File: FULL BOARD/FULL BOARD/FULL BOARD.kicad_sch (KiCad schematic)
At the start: 72 parts, among them J1 PJ-036AH-SMT-TR, J2 Micro_SD_Card, J3 Conn_01x04_Male, SW1 SW_Push, U1 LD1117S33TR_SOT223, U2 STM32H743VITx, Y1 16Mhz

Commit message: schematic done
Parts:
- removed FB1: FerriteBead, symbol Device:FerriteBead
- removed J3: Conn_01x04_Male, symbol Connector:Conn_01x04_Male
- removed Y1: 16Mhz, symbol Device:Crystal_GND24
- added FL1: BLM15GA750SZ1D, footprints:BEADC1005X55N, symbol BLM15GA750SZ1D:BLM15GA750SZ1D
- added J4: 5019514000, footprints:CON_5019514000, symbol 2024-09-26_21-43-55:5019514000
- added J5: 61201021621, footprints:CONN_61201021621_WRE, symbol 2024-09-27_18-41-52:61201021621
- added R4, R5, R6, R7: 1k, Resistor_SMD:R_0805_2012Metric, symbol Device:R_US
- added Y1: ABLS7M2-16.000MHZ-D-2Y-T, footprints:XTAL_ABLS7M2-16.000MHZ-D-2Y-T, symbol ABLS7M2-16.000MHZ-D-2Y-T:ABLS7M2-16.000MHZ-D-2Y-T
- C1, C15, C4: footprint (none) -> Capacitor_SMD:C_0805_2012Metric
- C10, C11, C12, C13, C14, C16, C17, C18, C19, C20, C5, C6, C9: footprint (none) -> Capacitor_SMD:C_0402_1005Metric
- C2, C7, C8: footprint Capacitor_SMD:C_0805_2012Metric_Pad1.15x1.40mm_HandSolder -> Capacitor_SMD:C_0402_1005Metric
- C3: footprint (none) -> Capacitor_SMD:C_0603_1608Metric
- D1, D10, D11, D12, D13, D14, D15, D16, D17, D18, D19, D2, D20, D3, D4, D5, D6, D7, D8, D9: footprint ScottoKeebs_Components:Diode_DO-35 -> Keyboard footprint:Diode_DO-35
- R1, R2, R3: footprint Resistor_SMD:R_0805_2012Metric_Pad1.15x1.40mm_HandSolder -> Resistor_SMD:R_0805_2012Metric
- S1, S10, S11, S12, S13, S14, S15, S16, S17, S18, S19, S2, S20, S3, S4, S5, S6, S7, S8, S9: footprint ScottoKeebs_MX:MX_PCB_1.00u -> Keyboard footprint:MX_PCB_1.00u
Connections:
- net +3.3V: now also FL1.2
- net +3.3VA: now also FL1.1
- net Col 1: now also R4.2; no longer S1.1, S13.1, S17.1, S5.1, S9.1
- net Col 2: now also R5.2; no longer S10.1, S14.1, S18.1, S2.1, S6.1
- net Col 3: now also R6.2; no longer S11.1, S15.1, S19.1, S3.1, S7.1
- net Col 4: now also R7.2; no longer S12.1, S16.1, S20.1, S4.1, S8.1
- net GND: now also J5.3, J5.4
- net HSE_IN: now also Y1.1
- net HSE_OUT: now also Y1.2
- net NRST: now also J5.1
- net SWC: now also J5.6
- net SWDIO: now also J5.2
- net LCD_CS: now reaches U2.28 (PA4)
- net LCD_CS: now also J4.5
- net LCD_SCK: now reaches U2.29 (PA5)
- net LCD_SCK: now also J4.8
- net LCD_MISO: now reaches U2.30 (PA6)
- net LCD_MISO: now also J4.6
- net LCD_MOSI: now reaches U2.31 (PA7)
- net LCD_MOSI: now also J4.7
- new net: R5.1, S10.1, S14.1, S18.1, S2.1, S6.1
- new net: R6.1, S11.1, S15.1, S19.1, S3.1, S7.1
- new net: R4.1, S1.1, S13.1, S17.1, S5.1, S9.1
- new net: R7.1, S12.1, S16.1, S20.1, S4.1, S8.1
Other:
- moved on the sheet: C1, C10, C11, C12, C14, C15, C16, C17, C18, C19, C20, C3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

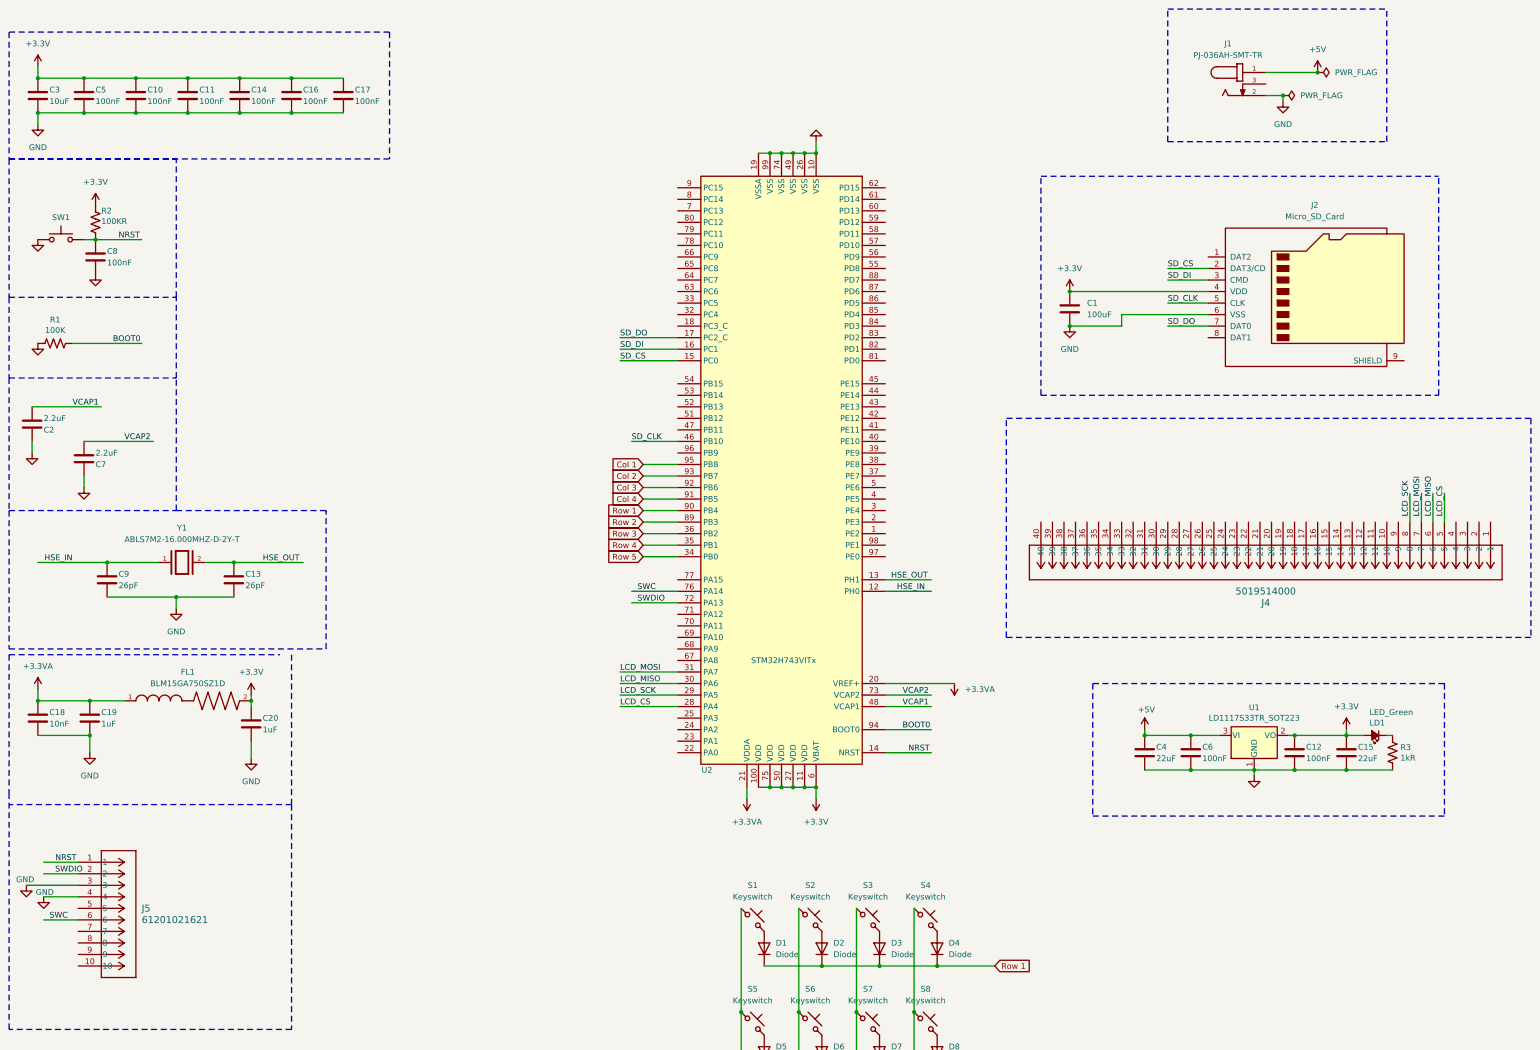
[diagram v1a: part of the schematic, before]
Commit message: schematics done with errors checked
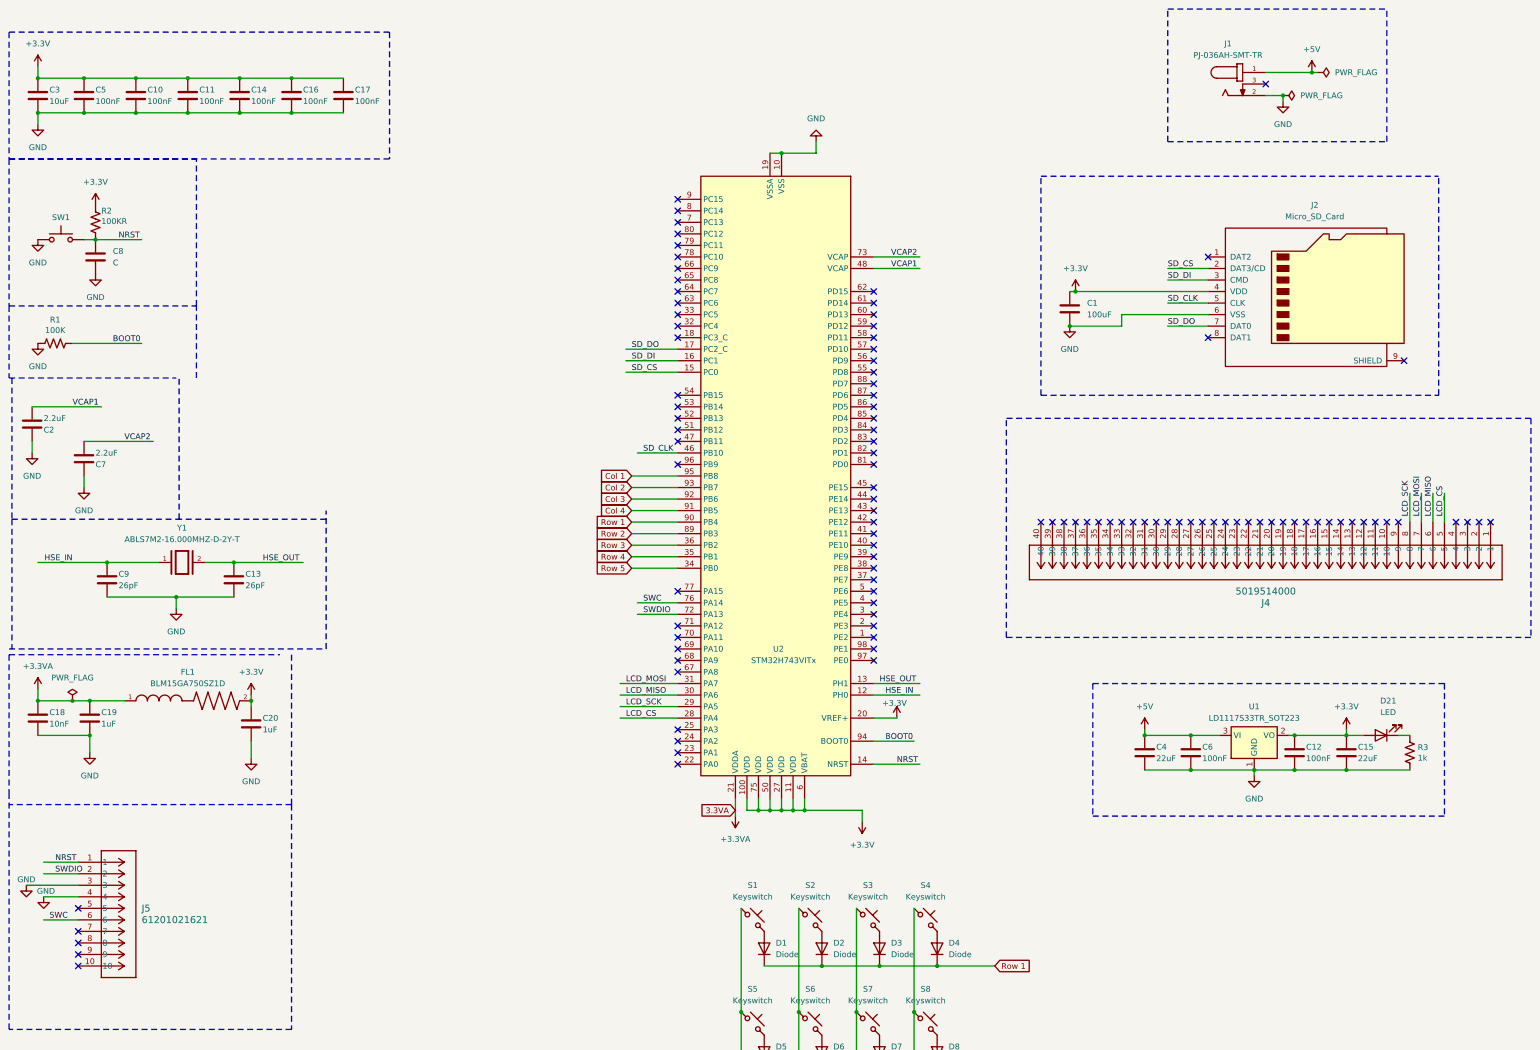
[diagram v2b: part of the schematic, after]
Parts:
- removed LD1: LED_Green, LED_SMD:LED_0805_2012Metric, symbol stm32f091-rescue:LED_Small_ALT-Device
- added D21: LED, symbol Device:LED
- C8: value 100nF -> C; footprint Capacitor_SMD:C_0402_1005Metric -> (none)
- R3: value 1kR -> 1k
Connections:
- net +3.3V: now also U2.20 (VREF+), D21.2 (A)
- net +3.3VA: no longer U2.20 (VREF+)
- net at R3.1: now also D21.1 (K)
- no-connect marks 0 -> 106
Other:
- moved on the sheet: R3

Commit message: schematics done with errors checked1
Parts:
- R2: value 100KR -> 100k
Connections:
- net +5V: now also J4.1, J4.2, J4.37, J4.38
- net GND: now also J4.13, J4.3, J4.31, J4.39, J4.4, J4.40
- no-connect marks 106 -> 96

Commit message: amp schematic added
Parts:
- added C21, C22, C23, C24, C26: 1uF, Capacitor_SMD:C_0402_1005Metric, symbol Device:C
- added C25, C31, C33: 10uF, Capacitor_SMD:C_0402_1005Metric, symbol Device:C
- added C27, C28, C29, C30: .22uF, Capacitor_SMD:C_0402_1005Metric, symbol Device:C
- added IC1: TAS5760LDAP, SOP65P810X120-33N, symbol TAS5760LDAP:TAS5760LDAP
- added J3, J6: Conn_01x02_Socket, symbol Connector:Conn_01x02_Socket
- added R8: 47, Resistor_SMD:R_0805_2012Metric, symbol Device:R_US
- added R9: 10k, Resistor_SMD:R_0805_2012Metric, symbol Device:R_US
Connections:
- net +5V: now also C25.2, C31.2, C33.2, IC1.1 (AVDD), IC1.21 (PVDD_1), IC1.28 (PVDD_2)
- net GND: now also C23.1, C24.2, C25.1, C26.2, C31.1, C33.1, IC1.18 (DGND), IC1.22 (PGND_1), IC1.27 (PGND_2), IC1.31 (GGND), R8.2
- new net: C26.1, IC1.32 (GVDD_REG), R9.2
- new net: C23.2, IC1.2 (SFT_CLIP), R8.1, R9.1
- new net: C22.1, IC1.3 (ANA_REG)
- new net: C21.2, C22.2, IC1.5 (ANA_REF)
- new net: C28.2, IC1.20 (SPK_OUTB+), J6.1 (Pin_1)
- new net: C30.2, IC1.23 (SPK_OUTB-), J6.2 (Pin_2)
- new net: C24.1, IC1.10 (DVDD)
- new net: C28.1, IC1.19 (BSTRPB+)
- new net: C30.1, IC1.24 (BSTRPB-)
- new net: C29.1, IC1.25 (BSTRPA-)
- new net: C29.2, IC1.26 (SPK_OUTA-), J3.2 (Pin_2)
- new net: C27.2, IC1.29 (SPK_OUTA+), J3.1 (Pin_1)
- new net: C27.1, IC1.30 (BSTRPA+)
- new net: C21.1, IC1.4 (VCOM)
- new net I2S_CK: IC1.15 (SCLK)
- new net I2S_MCLK: IC1.14 (MCLK)
- new net I2S_SD: IC1.16 (SDIN)
- new net I2S_WS: IC1.17 (LRCK)
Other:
- moved on the sheet: D1, D10, D11, D12, D13, D14, D15, D16, D17, D18, D19, D2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

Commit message: some routing done
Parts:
- removed J3, J6: Conn_01x02_Socket, symbol Connector:Conn_01x02_Socket
- added D22, D23, D24: LED, LED_SMD:LED_0805_2012Metric, symbol Device:LED
- added J3, J6: B2B-PH-K-S, audiojack:CONN2_B2B-PH-K-S_JST, symbol B2B-PH-K-S:B2B-PH-K-S
- added R10, R11, R12: 10k, Resistor_SMD:R_0805_2012Metric, symbol Device:R_US
- C8: value C -> 100nF; footprint (none) -> Capacitor_SMD:C_0402_1005Metric
- D21: footprint (none) -> LED_SMD:LED_0805_2012Metric
- IC1: footprint SOP65P810X120-33N -> KiCad:SOP65P810X120-33N
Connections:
- net LCD_CS is gone; now on net I2S_WS: J4.5, U2.28 (PA4)
- net Col 1: now also U2.86 (PD5); no longer U2.95 (PB8)
- net Col 2: now also U2.87 (PD6); no longer U2.93 (PB7)
- net Col 3: now also U2.88 (PD7); no longer U2.92 (PB6)
- net Col 4: now also U2.89 (PB3); no longer U2.91 (PB5)
- net GND: now also D22.1 (K), D23.1 (K), D24.1 (K)
- net I2S_CK: now also U2.78 (PC10)
- net I2S_MCLK: now also U2.64 (PC7)
- net I2S_SD: now also U2.36 (PB2)
- net Row 1: now also U2.82 (PD1); no longer U2.90 (PB4)
- net Row 2: now also U2.83 (PD2); no longer U2.89 (PB3)
- net Row 3: now also U2.84 (PD3); no longer U2.36 (PB2)
- net Row 4: now also U2.85 (PD4); no longer U2.35 (PB1)
- net Row 5: now also U2.81 (PD0); no longer U2.34 (PB0)
- net at U2.1 (PE2): now also R12.1
- net at U2.97 (PE0): now also R11.1
- net at U2.98 (PE1): now also R10.1
- net at C28.2, IC1.20 (SPK_OUTB+): now also J6.1
- net at C30.2, IC1.23 (SPK_OUTB-): now also J6.2
- net at C29.2, IC1.26 (SPK_OUTA-): now also J3.2
- net at C27.2, IC1.29 (SPK_OUTA+): now also J3.1
- new net: D23.2 (A), R10.2
- new net: D24.2 (A), R11.2
- new net: D22.2 (A), R12.2
- no-connect marks 96 -> 83
